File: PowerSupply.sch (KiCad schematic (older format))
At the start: 58 parts, among them J1 Conn_01x03, J2 Conn_01x02, J22 Jack-DC, J23 Conn_01x02, J24 Conn_01x02, J25 Conn_01x01, J26 Conn_01x01, J27 Conn_01x01, J28 Conn_01x01, J3 Conn_01x02, J6 Conn_01x01, J7 Conn_01x01, J8 Conn_01x01, J9 Conn_01x01, Q1 2N3906, Q2 TIP41C, U1 LM317, U2 LM337

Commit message: JLCPCB order 2021-04-11
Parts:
- removed Q1: 2N3906, TO_SOT_Packages_THT:TO-92_Inline_Wide, symbol 2N3906
- removed Q2: TIP41C, TO_SOT_Packages_THT:TO-220-3_Vertical, symbol TIP41C
- added C63: 100 nF, Capacitors_THT:C_Disc_D5.0mm_W2.5mm_P5.00mm, symbol C_Small
- added JP3, JP4: PIN2, Pin_Headers:Pin_Header_Straight_1x02_Pitch2.54mm, symbol Jumper_NO_Small
- added Q1: 2N3904, TO_SOT_Packages_THT:TO-92_Inline_Wide, symbol 2N3904
- added Q2: TIP42C, TO_SOT_Packages_THT:TO-220-3_Vertical, symbol TIP42C
- added R45, R48: 100k, Resistors_THT:R_Axial_DIN0207_L6.3mm_D2.5mm_P7.62mm_Horizontal, symbol R
- added R46: 150R, Resistors_THT:R_Axial_DIN0309_L9.0mm_D3.2mm_P12.70mm_Horizontal, symbol R
- C4, C5: value 1500 uF -> 2200 uF
- R23: value 1k -> 3k3
- R42: value 10k -> 100k
- R43, R44: value 4R7 -> 1R
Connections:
- net +15V: now also Q2.3 (E), R45.1
- net -15V: now also Q1.1 (E), R46.1
- net GND: now also C63.1, JP3.1
- net at J24.1 (Pin_1), RLY7.2 (Pole): now also JP3.2
- net at J24.2 (Pin_2), RLY7.4 (NO): now also JP4.2
- net at D17.2 (A), R42.2: now also Q1.2 (B)
- net at D17.1 (K), R41.1: now also R48.1
- net at R23.2: now also Q2.1 (B), R45.2
- net at R23.1: now also Q1.3 (C)
- net at D18.1 (K), RLY10.5 (Coil), RLY11.5 (Coil)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: now also C63.2, Q2.2 (C), R48.2
- new net: JP4.1, R46.2
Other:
- moved on the sheet: D17, D18, R23, R41, R42

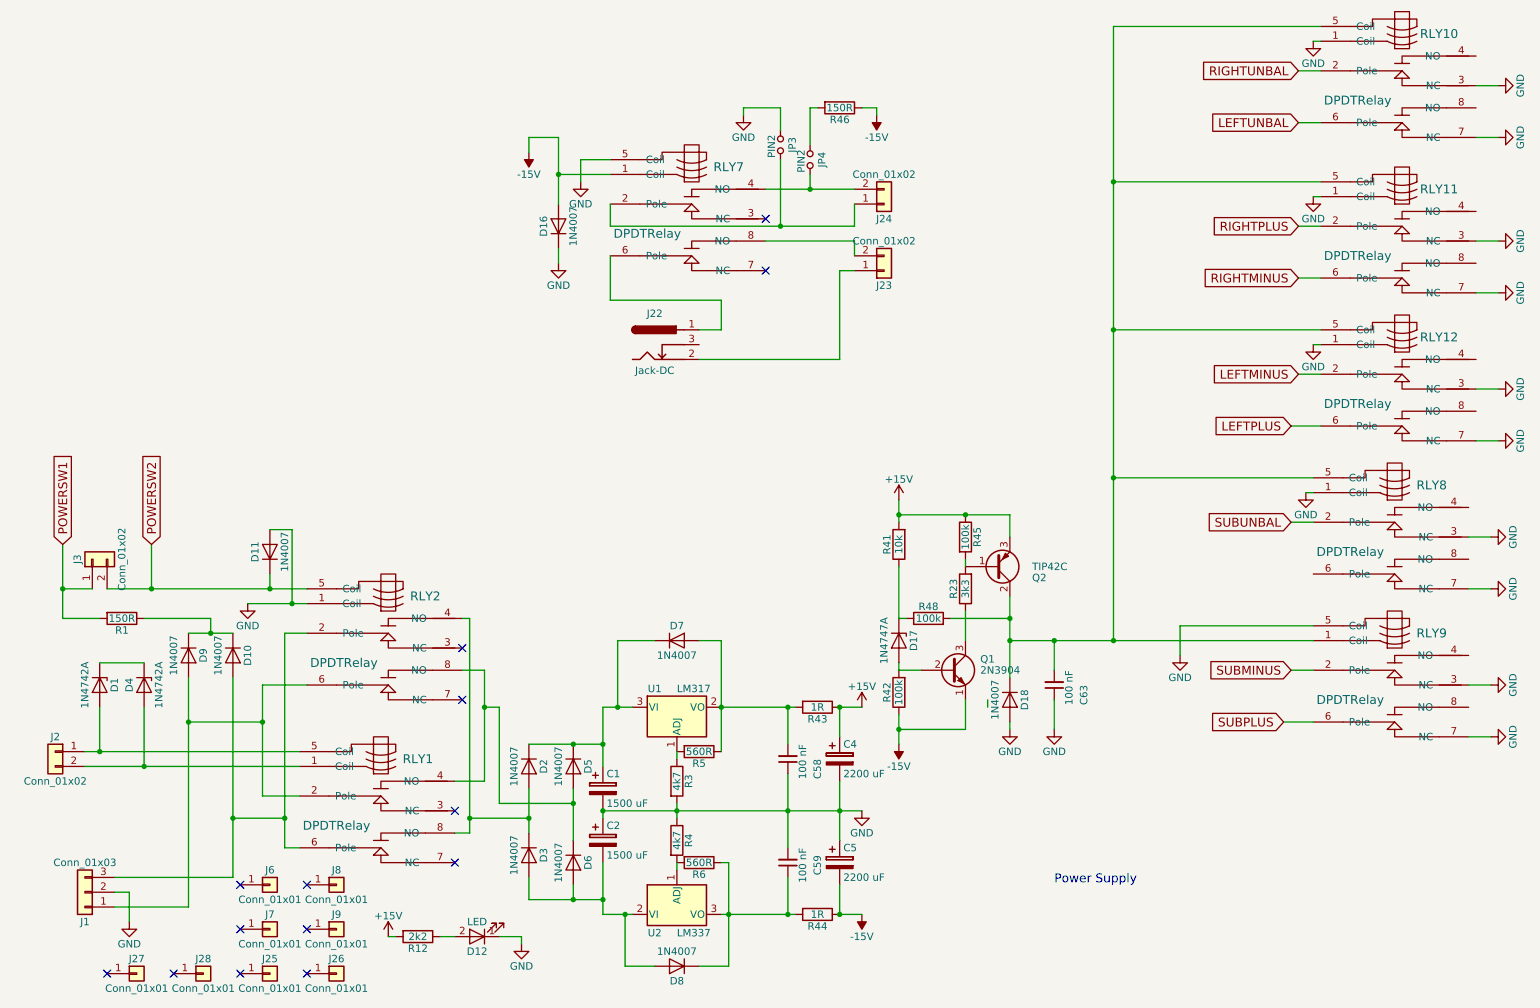
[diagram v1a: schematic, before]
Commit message: Moved around a component to make a little more space
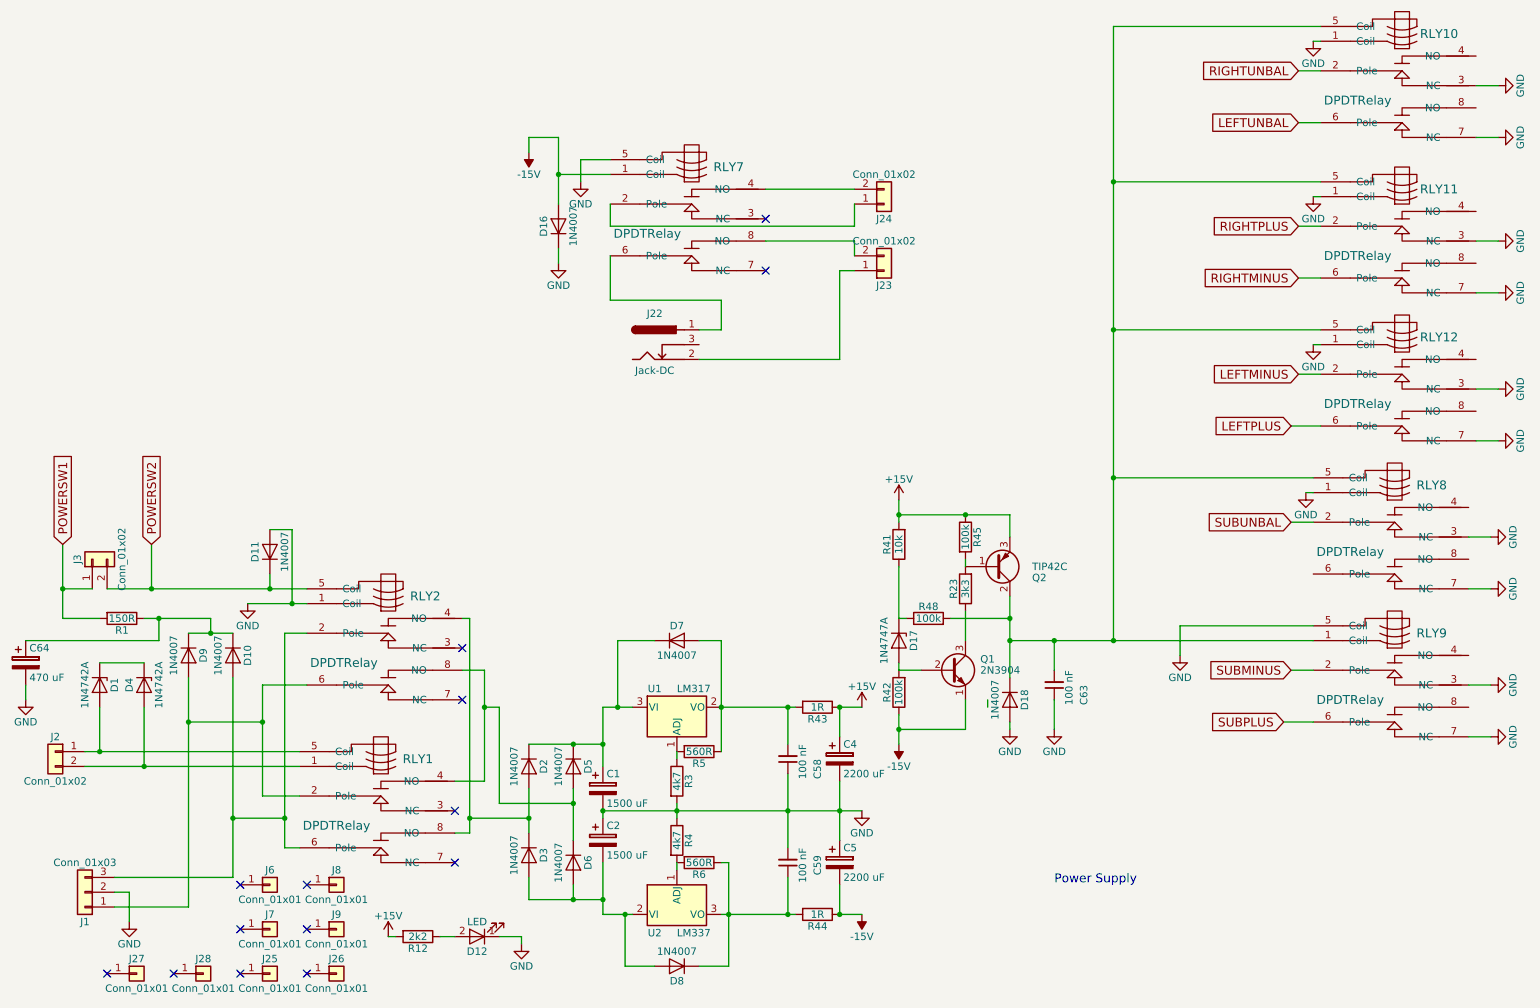
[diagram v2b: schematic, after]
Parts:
- removed JP3, JP4: PIN2, Pin_Headers:Pin_Header_Straight_1x02_Pitch2.54mm, symbol Jumper_NO_Small
- removed R46: 150R, Resistors_THT:R_Axial_DIN0309_L9.0mm_D3.2mm_P12.70mm_Horizontal, symbol R
- added C64: 470 uF, Capacitors_THT:CP_Radial_D10.0mm_P5.00mm, symbol CP
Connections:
- net GND: now also C64.2
- net at D10.1 (K), D9.1 (K), R1.1: now also C64.1
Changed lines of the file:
@@
 $EndComp
 $Comp
-L GND #PWR80
+L GND #PWR81
 U 1 1 606D5FED
 P 1350 7050
-F 0 "#PWR80" H 1350 6800 50  0001 C CNN
+F 0 "#PWR81" H 1350 6800 50  0001 C CNN
 F 1 "GND" H 1350 6900 50  0000 C CNN
 F 2 "" H 1350 7050 50  0001 C CNN
@@
 $EndComp
 $Comp
-L GND #PWR81
+L GND #PWR82
 U 1 1 606D606A
 P 2150 4900
-F 0 "#PWR81" H 2150 4650 50  0001 C CNN
+F 0 "#PWR82" H 2150 4650 50  0001 C CNN
 F 1 "GND" H 2150 4750 50  0000 C CNN
 F 2 "" H 2150 4900 50  0001 C CNN
@@
 $EndComp
 $Comp
-L GND #PWR83
+L GND #PWR84
 U 1 1 606D6085
 P 4000 7200
-F 0 "#PWR83" H 4000 6950 50  0001 C CNN
+F 0 "#PWR84" H 4000 6950 50  0001 C CNN
 F 1 "GND" H 4000 7050 50  0000 C CNN
 F 2 "" H 4000 7200 50  0001 C CNN
@@
 Power Supply
 $Comp
-L GND #PWR94
+L GND #PWR93
 U 1 1 606DF2B7
 P 7300 5750
-F 0 "#PWR94" H 7300 5500 50  0001 C CNN
+F 0 "#PWR93" H 7300 5500 50  0001 C CNN
 F 1 "GND" H 7300 5600 50  0000 C CNN
 F 2 "" H 7300 5750 50  0001 C CNN
@@
 SUBUNBAL
 $Comp
-L GND #PWR105
+L GND #PWR104
 U 1 1 606F678E
 P 10600 1400
-F 0 "#PWR105" H 10600 1150 50  0001 C CNN
+F 0 "#PWR104" H 10600 1150 50  0001 C CNN
 F 1 "GND" H 10600 1250 50  0000 C CNN
 F 2 "" H 10600 1400 50  0001 C CNN
@@
 $EndComp
 $Comp
-L GND #PWR106
+L GND #PWR105
 U 1 1 606F6A81
 P 10600 1750
-F 0 "#PWR106" H 10600 1500 50  0001 C CNN
+F 0 "#PWR105" H 10600 1500 50  0001 C CNN
 F 1 "GND" H 10600 1600 50  0000 C CNN
 F 2 "" H 10600 1750 50  0001 C CNN
@@
 $EndComp
 $Comp
-L GND #PWR98
+L GND #PWR97
 U 1 1 606F6F41
 P 9350 1100
-F 0 "#PWR98" H 9350 850 50  0001 C CNN
+F 0 "#PWR97" H 9350 850 50  0001 C CNN
 F 1 "GND" H 9350 950 50  0000 C CNN
 F 2 "" H 9350 1100 50  0001 C CNN
@@
 $EndComp
 $Comp
-L GND #PWR107
+L GND #PWR106
 U 1 1 606F7436
 P 10600 2450
-F 0 "#PWR107" H 10600 2200 50  0001 C CNN
+F 0 "#PWR106" H 10600 2200 50  0001 C CNN
 F 1 "GND" H 10600 2300 50  0000 C CNN
 F 2 "" H 10600 2450 50  0001 C CNN
@@
 $EndComp
 $Comp
-L GND #PWR108
+L GND #PWR107
 U 1 1 606F7669
 P 10600 2800
-F 0 "#PWR108" H 10600 2550 50  0001 C CNN
+F 0 "#PWR107" H 10600 2550 50  0001 C CNN
 F 1 "GND" H 10600 2650 50  0000 C CNN
 F 2 "" H 10600 2800 50  0001 C CNN
@@
 $EndComp
 $Comp
-L GND #PWR109
+L GND #PWR108
 U 1 1 606F84BF
 P 10600 3450
-F 0 "#PWR109" H 10600 3200 50  0001 C CNN
+F 0 "#PWR108" H 10600 3200 50  0001 C CNN
 F 1 "GND" H 10600 3300 50  0000 C CNN
 F 2 "" H 10600 3450 50  0001 C CNN
@@
 $EndComp
 $Comp
-L GND #PWR110
+L GND #PWR109
 U 1 1 606F8632
 P 10600 3800
-F 0 "#PWR110" H 10600 3550 50  0001 C CNN
+F 0 "#PWR109" H 10600 3550 50  0001 C CNN
 F 1 "GND" H 10600 3650 50  0000 C CNN
 F 2 "" H 10600 3800 50  0001 C CNN
@@
 $EndComp
 $Comp
-L GND #PWR101
+L GND #PWR100
 U 1 1 606F8F91
 P 10550 4450
-F 0 "#PWR101" H 10550 4200 50  0001 C CNN
+F 0 "#PWR100" H 10550 4200 50  0001 C CNN
 F 1 "GND" H 10550 4300 50  0000 C CNN
 F 2 "" H 10550 4450 50  0001 C CNN
@@
 $EndComp
 $Comp
-L GND #PWR102
+L GND #PWR101
 U 1 1 606F910C
 P 10550 4800
-F 0 "#PWR102" H 10550 4550 50  0001 C CNN
+F 0 "#PWR101" H 10550 4550 50  0001 C CNN
 F 1 "GND" H 10550 4650 50  0000 C CNN
 F 2 "" H 10550 4800 50  0001 C CNN
@@
 $EndComp
 $Comp
-L GND #PWR99
+L GND #PWR98
 U 1 1 606F9F16
 P 9350 2150
-F 0 "#PWR99" H 9350 1900 50  0001 C CNN
+F 0 "#PWR98" H 9350 1900 50  0001 C CNN
 F 1 "GND" H 9350 2000 50  0000 C CNN
 F 2 "" H 9350 2150 50  0001 C CNN
@@
 $EndComp
 $Comp
-L GND #PWR100
+L GND #PWR99
 U 1 1 606FA0A1
 P 9350 3150
-F 0 "#PWR100" H 9350 2900 50  0001 C CNN
+F 0 "#PWR99" H 9350 2900 50  0001 C CNN
 F 1 "GND" H 9350 3000 50  0000 C CNN
 F 2 "" H 9350 3150 50  0001 C CNN
@@
 $EndComp
 $Comp
-L GND #PWR97
+L GND #PWR96
 U 1 1 606FA305
 P 9300 4150
-F 0 "#PWR97" H 9300 3900 50  0001 C CNN
+F 0 "#PWR96" H 9300 3900 50  0001 C CNN
 F 1 "GND" H 9300 4000 50  0000 C CNN
 F 2 "" H 9300 4150 50  0001 C CNN
@@
 $EndComp
 $Comp
-L GND #PWR103
+L GND #PWR102
 U 1 1 606FAB7E
 P 10550 5450
-F 0 "#PWR103" H 10550 5200 50  0001 C CNN
+F 0 "#PWR102" H 10550 5200 50  0001 C CNN
 F 1 "GND" H 10550 5300 50  0000 C CNN
 F 2 "" H 10550 5450 50  0001 C CNN
@@
 $EndComp
 $Comp
-L GND #PWR104
+L GND #PWR103
 U 1 1 606FAD7D
 P 10550 5800
-F 0 "#PWR104" H 10550 5550 50  0001 C CNN
+F 0 "#PWR103" H 10550 5550 50  0001 C CNN
 F 1 "GND" H 10550 5650 50  0000 C CNN
 F 2 "" H 10550 5800 50  0001 C CNN
@@
 $EndComp
 $Comp
-L GND #PWR86
+L GND #PWR87
 U 1 1 606FCAFD
 P 4400 2050
-F 0 "#PWR86" H 4400 1800 50  0001 C CNN
+F 0 "#PWR87" H 4400 1800 50  0001 C CNN
 F 1 "GND" H 4400 1900 50  0000 C CNN
 F 2 "" H 4400 2050 50  0001 C CNN
@@
 $EndComp
 $Comp
-L -15V #PWR93
+L -15V #PWR92
 U 1 1 607050A0
 P 6550 5850
-F 0 "#PWR93" H 6550 5950 50  0001 C CNN
+F 0 "#PWR92" H 6550 5950 50  0001 C CNN
 F 1 "-15V" H 6550 6000 50  0000 C CNN
 F 2 "" H 6550 5850 50  0001 C CNN
@@
 $EndComp
 $Comp
-L +15V #PWR92
+L +15V #PWR91
 U 1 1 60705366
 P 6550 4200
-F 0 "#PWR92" H 6550 4050 50  0001 C CNN
+F 0 "#PWR91" H 6550 4050 50  0001 C CNN
 F 1 "+15V" H 6550 4340 50  0000 C CNN
 F 2 "" H 6550 4200 50  0001 C CNN
@@
 $EndComp
 $Comp
-L +15V #PWR82
+L +15V #PWR83
 U 1 1 60705AF1
 P 3100 7150
-F 0 "#PWR82" H 3100 7000 50  0001 C CNN
+F 0 "#PWR83" H 3100 7000 50  0001 C CNN
 F 1 "+15V" H 3100 7290 50  0000 C CNN
 F 2 "" H 3100 7150 50  0001 C CNN
@@
 $EndComp
 $Comp
-L GND #PWR85
+L GND #PWR86
 U 1 1 60706D8C
 P 4250 2600
-F 0 "#PWR85" H 4250 2350 50  0001 C CNN
+F 0 "#PWR86" H 4250 2350 50  0001 C CNN
 F 1 "GND" H 4250 2450 50  0000 C CNN
 F 2 "" H 4250 2600 50  0001 C CNN
@@
 $EndComp
 $Comp
-L -15V #PWR84
+L -15V #PWR85
 U 1 1 607072F3
 P 4050 1850
-F 0 "#PWR84" H 4050 1950 50  0001 C CNN
+F 0 "#PWR85" H 4050 1950 50  0001 C CNN
 F 1 "-15V" H 4050 2000 50  0000 C CNN
 F 2 "" H 4050 1850 50  0001 C CNN
@@
 $EndComp
 $Comp
-L GND #PWR96
+L GND #PWR95
 U 1 1 6070A0C7
 P 8450 5250
-F 0 "#PWR96" H 8450 5000 50  0001 C CNN
+F 0 "#PWR95" H 8450 5000 50  0001 C CNN
 F 1 "GND" H 8450 5100 50  0000 C CNN
 F 2 "" H 8450 5250 50  0001 C CNN
@@
 $EndComp
 $Comp
-L Jumper_NO_Small JP4
-U 1 1 60727791
-P 5950 1900
-F 0 "JP4" H 5950 1980 50  0000 C CNN
-F 1 "PIN2" H 5960 1840 50  0000 C CNN
-F 2 "Pin_Headers:Pin_Header_Straight_1x02_Pitch2.54mm" H 5950 1900 50  0001 C CNN
-F 3 "" H 5950 1900 50  0001 C CNN
-	1    5950 1900
-	0    1    1    0
-$EndComp
-$Comp
-L -15V #PWR91
-U 1 1 60727F8C
-P 6400 1600
-F 0 "#PWR91" H 6400 1700 50  0001 C CNN
-F 1 "-15V" H 6400 1750 50  0000 C CNN
-F 2 "" H 6400 1600 50  0001 C CNN
-F 3 "" H 6400 1600 50  0001 C CNN
-	1    6400 1600
-	-1   0    0    1
-$EndComp
-$Comp
-L Jumper_NO_Small JP3
-U 1 1 607282EE
-P 5750 1800
-F 0 "JP3" H 5750 1880 50  0000 C CNN
-F 1 "PIN2" H 5760 1740 50  0000 C CNN
-F 2 "Pin_Headers:Pin_Header_Straight_1x02_Pitch2.54mm" H 5750 1800 50  0001 C CNN
-F 3 "" H 5750 1800 50  0001 C CNN
-	1    5750 1800
-	0    1    1    0
-$EndComp
-$Comp
-L GND #PWR87
-U 1 1 6072860E
-P 5500 1600
-F 0 "#PWR87" H 5500 1350 50  0001 C CNN
-F 1 "GND" H 5500 1450 50  0000 C CNN
-F 2 "" H 5500 1600 50  0001 C CNN
-F 3 "" H 5500 1600 50  0001 C CNN
-	1    5500 1600
-	1    0    0    -1
-$EndComp
-$Comp
-L R R46
-U 1 1 6072901E
-P 6150 1550
-F 0 "R46" V 6230 1550 50  0000 C CNN
-F 1 "150R" V 6150 1550 50  0000 C CNN
-F 2 "Resistors_THT:R_Axial_DIN0309_L9.0mm_D3.2mm_P12.70mm_Horizontal" V 6080 1550 50  0001 C CNN
-F 3 "" H 6150 1550 50  0001 C CNN
-	1    6150 1550
-	0    1    1    0
-$EndComp
-$Comp
 L C_Small C63
 U 1 1 607B24A7
@@
 $EndComp
 $Comp
-L GND #PWR95
+L GND #PWR94
 U 1 1 607B2586
 P 7600 5750
-F 0 "#PWR95" H 7600 5500 50  0001 C CNN
+F 0 "#PWR94" H 7600 5500 50  0001 C CNN
 F 1 "GND" H 7600 5600 50  0000 C CNN
 F 2 "" H 7600 5750 50  0001 C CNN
@@
 Wire Wire Line
 	7000 5750 7000 5550
-Wire Wire Line
-	5950 2000 5950 2100
-Connection ~ 5950 2100
-Wire Wire Line
-	5950 1550 5950 1800
-Wire Wire Line
-	5750 1700 5750 1550
-Wire Wire Line
-	5750 1550 5500 1550
-Wire Wire Line
-	5500 1550 5500 1600
-Wire Wire Line
-	6400 1550 6400 1600
-Wire Wire Line
-	6400 1550 6300 1550
-Wire Wire Line
-	6000 1550 5950 1550
-Wire Wire Line
-	5750 1900 5750 2350
-Connection ~ 5750 2350
 Connection ~ 7600 5150
 Wire Wire Line
@@
 Wire Wire Line
 	7600 5550 7600 5750
+$Comp
+L CP C64
+U 1 1 6084343E
+P 650 5300
+F 0 "C64" H 675 5400 50  0000 L CNN
+F 1 "470 uF" H 675 5200 50  0000 L CNN
+F 2 "Capacitors_THT:CP_Radial_D10.0mm_P5.00mm" H 688 5150 50  0001 C CNN
+F 3 "" H 650 5300 50  0001 C CNN
+	1    650  5300
+	1    0    0    -1
+$EndComp
+$Comp
+L GND #PWR80
+U 1 1 60843522
+P 650 5550
+F 0 "#PWR80" H 650 5300 50  0001 C CNN
+F 1 "GND" H 650 5400 50  0000 C CNN
+F 2 "" H 650 5550 50  0001 C CNN
+F 3 "" H 650 5550 50  0001 C CNN
+	1    650  5550
+	1    0    0    -1
+$EndComp
+Wire Wire Line
+	650  5550 650  5450
+Wire Wire Line
+	1550 5000 1550 5150
+Wire Wire Line
+	1550 5150 650  5150
+Connection ~ 1550 5000
 $EndSCHEMATC
